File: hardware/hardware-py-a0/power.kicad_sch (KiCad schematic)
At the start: 20 parts, among them Q1 AO3401A, Q2 AO3401A, U1 LTC4054ES5-4.2, U2 STI3411A, U6 XC6206PxxxMR

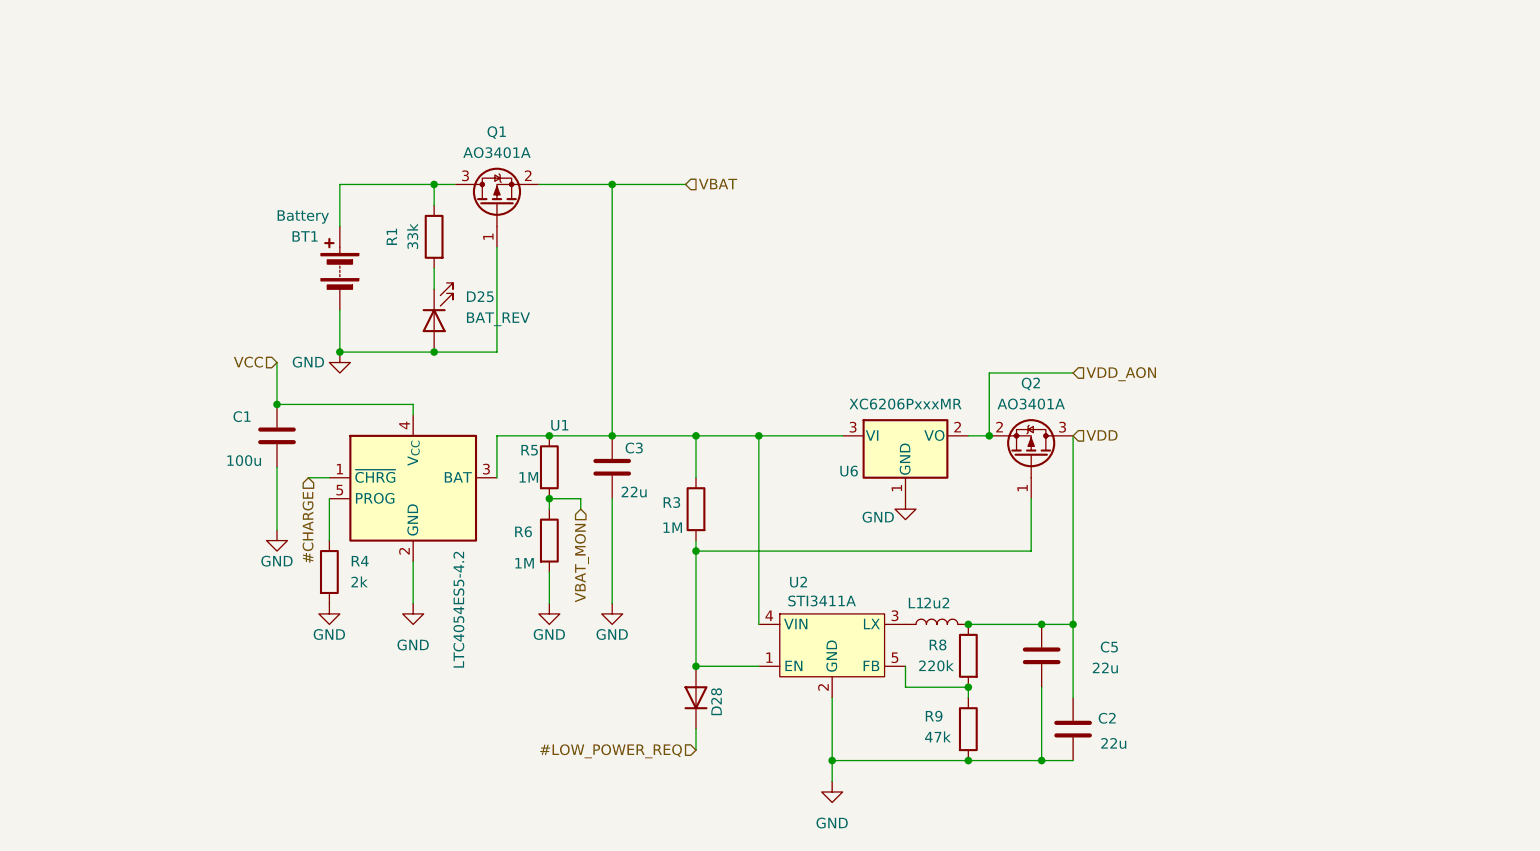
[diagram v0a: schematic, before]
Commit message: hardware: py/a0 revision 1.1 using FFC connectors
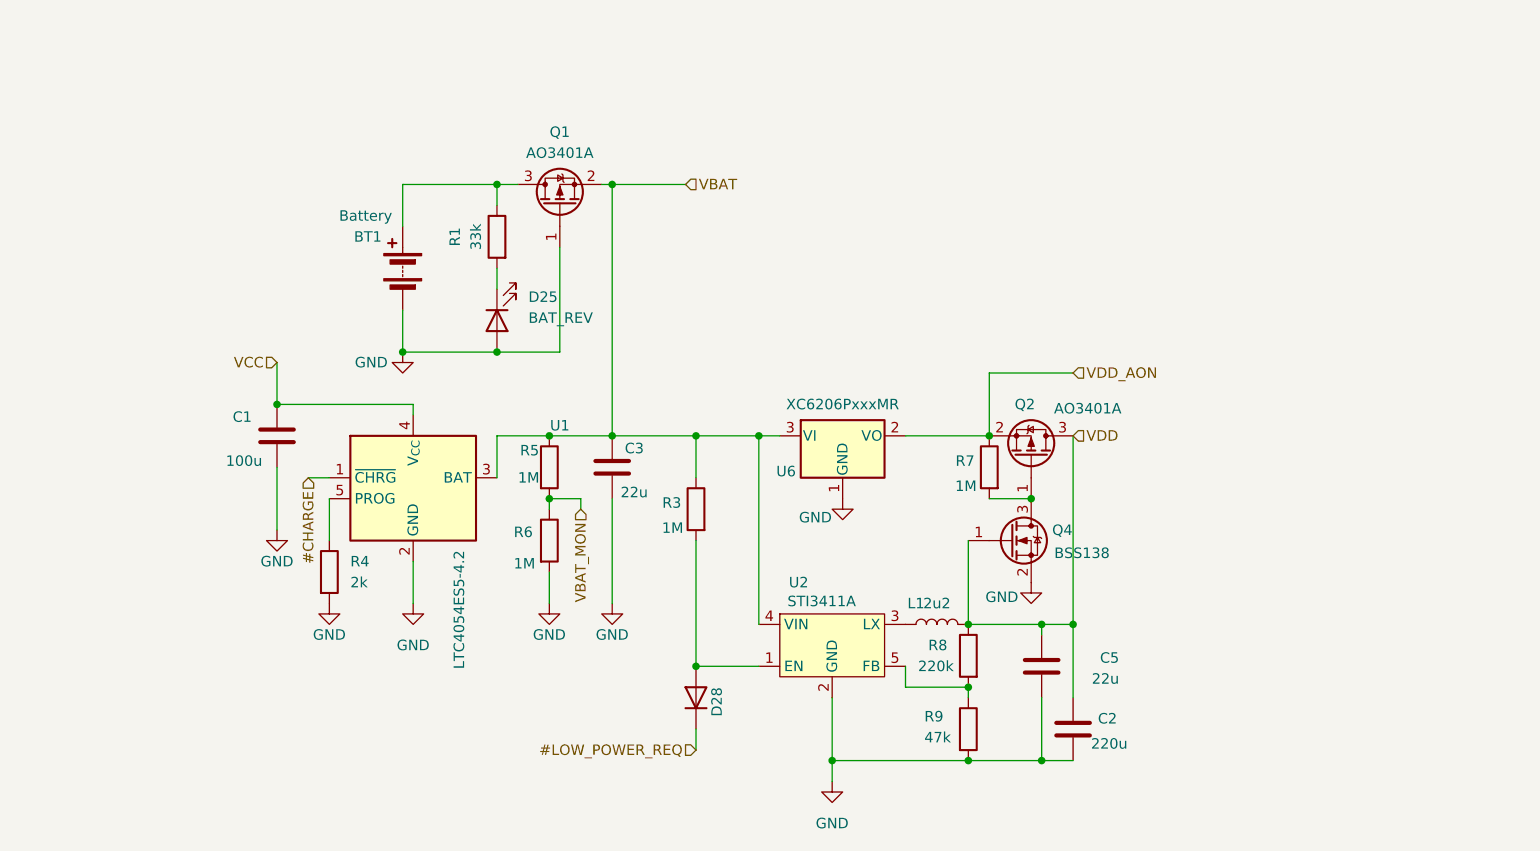
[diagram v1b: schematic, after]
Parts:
- added Q4: BSS138, Package_TO_SOT_SMD:SOT-23, symbol Transistor_FET:BSS138
- added R7: 1M, Resistor_SMD:R_0805_2012Metric_Pad1.20x1.40mm_HandSolder, symbol Device:R
- C2: value 22u -> 220u; footprint Resistor_SMD:R_1210_3225Metric_Pad1.30x2.65mm_HandSolder -> Capacitor_SMD:C_2220_5750Metric
- D25: footprint Resistor_SMD:R_0805_2012Metric_Pad1.20x1.40mm_HandSolder -> Diode_SMD:D_1206_3216Metric
- D28: footprint Diode_SMD:D_0805_2012Metric_Pad1.15x1.40mm_HandSolder -> Diode_SMD:D_1206_3216Metric
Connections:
- net GND: now also Q4.2 (S)
- net VDD: now also Q4.1 (G)
- net VDD_AON: now also R7.1
- net at D28.2 (A), R3.2, U2.1 (EN): no longer Q2.1 (G)
- new net: Q2.1 (G), Q4.3 (D), R7.2
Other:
- company: (none) -> MOTIV.PW
- moved on the sheet: BT1, C5, D25, Q1, R1, U6

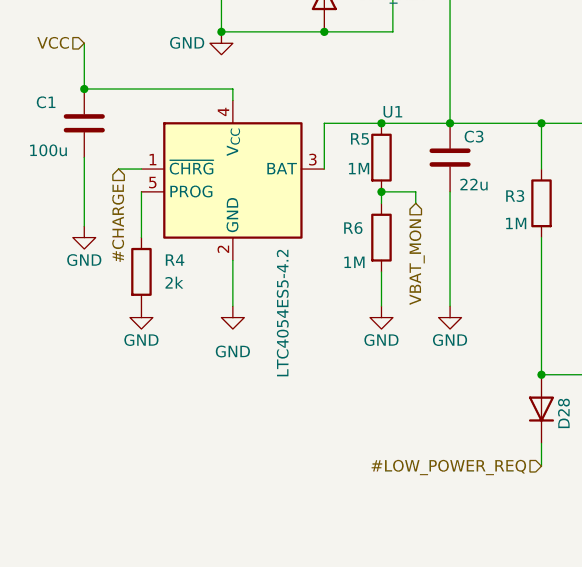
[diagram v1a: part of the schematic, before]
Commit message: terminal:os.dupterm Stream support
move files and rename folders to board_src and scripts
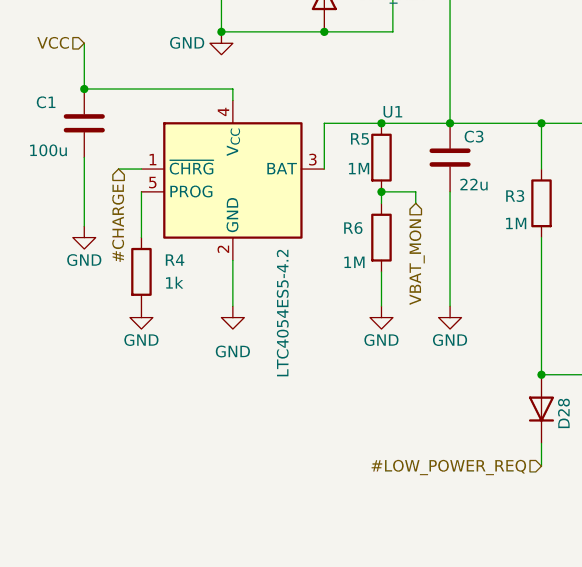
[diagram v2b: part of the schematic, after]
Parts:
- R4: value 2k -> 1k
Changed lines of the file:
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@@
 			)
 		)
-		(property "Value" "2k"
+		(property "Value" "1k"
 			(at 119.38 110.49 0)
 			(effects

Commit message: hw: power management begin
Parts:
- added Q3: BSS138, Package_TO_SOT_SMD:SOT-23, symbol Transistor_FET:BSS138
- R5, R6: value 1M -> 33k
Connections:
- net GND: now also Q3.2 (S); no longer R6.2
- net at D28.2 (A), R3.2, U2.1 (EN): now also Q3.1 (G)
- new net: Q3.3 (D), R6.2
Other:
- moved on the sheet: BT1, D25, Q1, R1

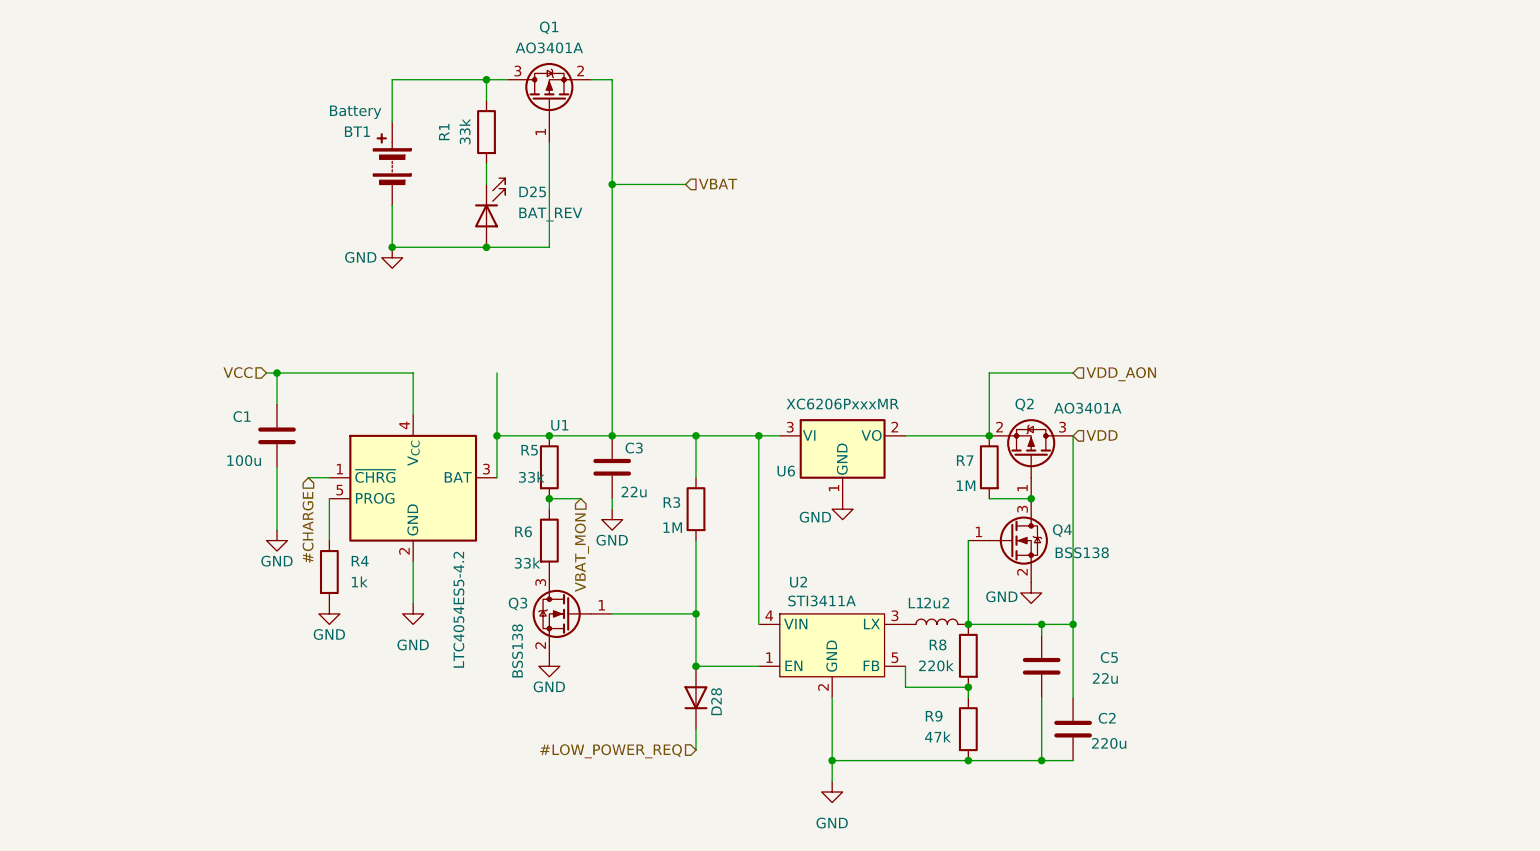
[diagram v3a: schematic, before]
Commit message: hw: testing power switch solution
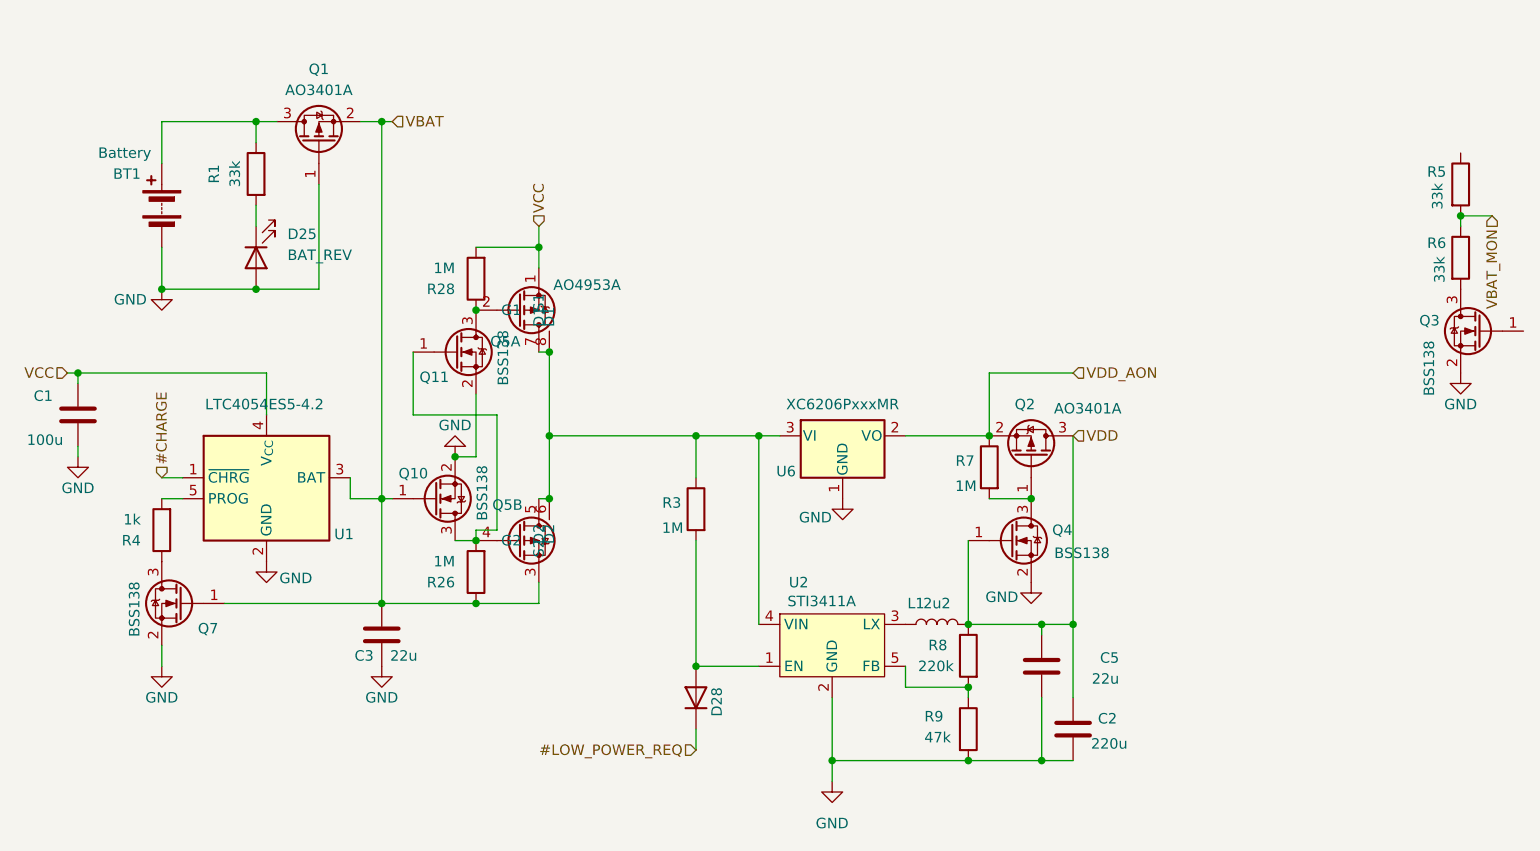
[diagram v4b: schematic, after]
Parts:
- added Q10, Q11, Q7: BSS138, Package_TO_SOT_SMD:SOT-23, symbol Transistor_FET:BSS138
- added Q5: AO4953A, Package_SO:SOP-8_3.9x4.9mm_P1.27mm, symbol custom:AO4953A
- added R26, R28: 1M, Resistor_SMD:R_0805_2012Metric_Pad1.20x1.40mm_HandSolder, symbol Device:R
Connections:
- net GND: now also Q10.2 (S), Q11.2 (S), Q7.2 (S); no longer R4.2
- net VBAT: now also Q10.1 (G), Q5.3 (S2), Q7.1 (G), R26.1; no longer R3.1, R5.1, U2.4 (VIN), U6.3 (VI)
- net VCC: now also Q5.1 (S1), R28.2
- net at U1.5 (PROG): now also R4.2; no longer R4.1
- net at D28.2 (A), R3.2, U2.1 (EN): no longer Q3.1 (G)
- new net: Q7.3 (D), R4.1
- new net: Q10.3 (D), Q11.1 (G), Q5.4 (G2), R26.2
- new net: Q5.5 (D2), Q5.6 (D2), Q5.7 (D1), Q5.8 (D1), R3.1, U2.4 (VIN), U6.3 (VI)
- new net: Q11.3 (D), Q5.2 (G1), R28.1
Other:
- moved on the sheet: BT1, C1, C3, D25, Q1, R1, R4, U1
